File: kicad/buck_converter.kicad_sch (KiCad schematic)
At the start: 47 parts, among them J5 SolderPad, J6 SolderPad, Q2 BSZ146N10LS5, Q3 BSZ146N10LS5, U2 LM5146

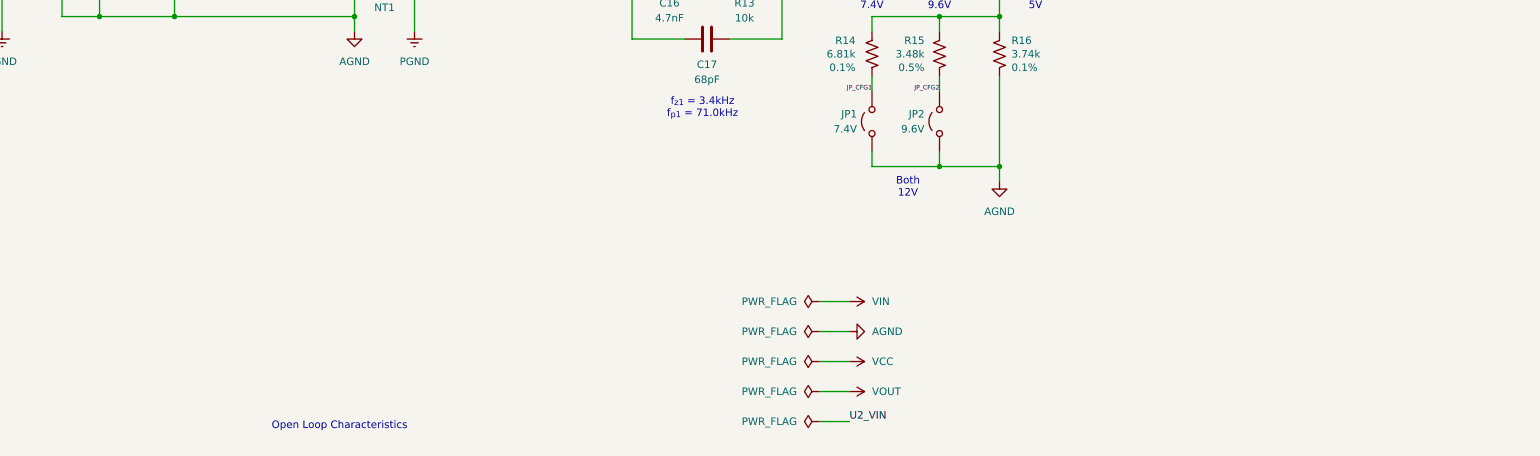
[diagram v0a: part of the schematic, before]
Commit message: Added UBCO trademark notice, prepared for production
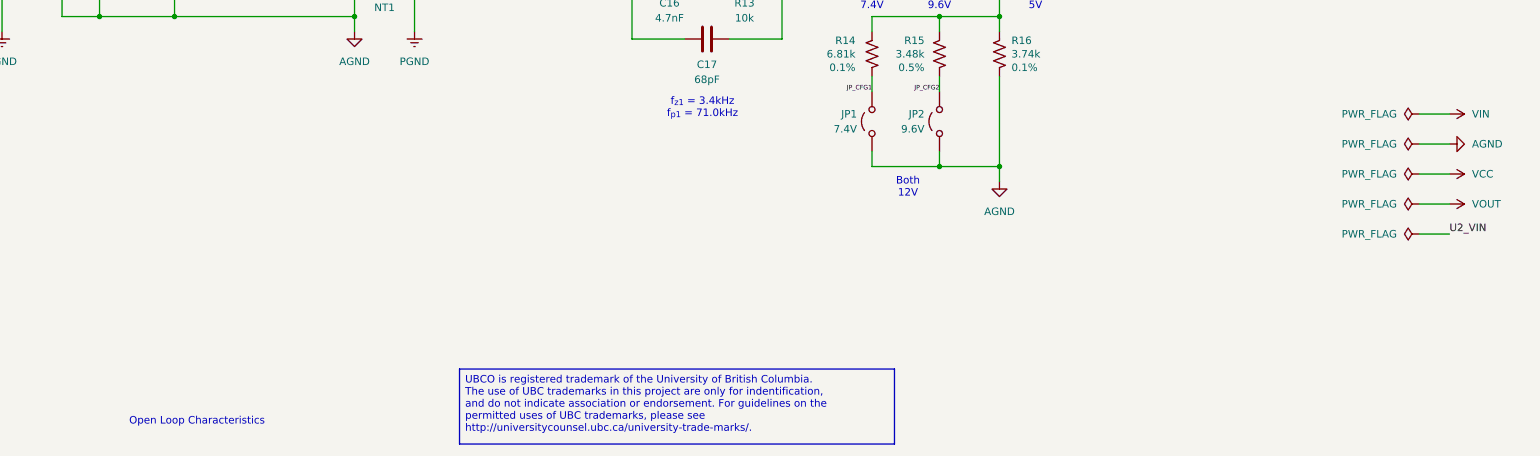
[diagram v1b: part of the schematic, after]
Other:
- company: Author: Julian Joaquin -> UBCO Aerospace
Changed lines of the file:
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@@
 		(date "2026-02-06")
 		(rev "D")
-		(company "Author: Julian Joaquin")
+		(company "UBCO Aerospace")
 		(comment 1 "Licensed under CERN-OHL-W version 2")
 		(comment 2 "Copyright © Julian Joaquin, 2026")
@@
 	(text "Open Loop Characteristics"
 		(exclude_from_sim no)
-		(at 80.01 192.532 0)
+		(at 55.88 191.77 0)
 		(effects
 			(font
@@
 		)
 	)
+	(text_box "UBCO is registered trademark of the University of British Columbia.\nThe use of UBC trademarks in this project are only for indentification,\nand do not indicate association or endorsement. For guidelines on the\npermitted uses of UBC trademarks, please see\nhttp://universitycounsel.ubc.ca/university-trade-marks/."
+		(exclude_from_sim no)
+		(at 100.33 182.88 0)
+		(size 73.66 12.7)
+		(margins 0.9525 0.9525 0.9525 0.9525)
+		(stroke
+			(width 0)
+			(type solid)
+			(color 132 0 0 1)
+		)
+		(fill
+			(type none)
+		)
+		(effects
+			(font
+				(size 1.27 1.27)
+				(color 132 0 0 1)
+			)
+			(justify left top)
+			(href "http://universitycounsel.ubc.ca/university-trade-marks")
+		)
+	)
 	(junction
 		(at 191.77 111.76)
@@
 	(wire
 		(pts
-			(xy 161.29 181.61) (xy 166.37 181.61)
+			(xy 262.89 149.86) (xy 267.97 149.86)
 		)
 		(stroke
@@
 	(wire
 		(pts
-			(xy 161.29 191.77) (xy 166.37 191.77)
+			(xy 262.89 160.02) (xy 267.97 160.02)
 		)
 		(stroke
@@
 	(wire
 		(pts
-			(xy 161.29 176.53) (xy 166.37 176.53)
+			(xy 262.89 144.78) (xy 267.97 144.78)
 		)
 		(stroke
@@
 	(wire
 		(pts
-			(xy 161.29 186.69) (xy 166.37 186.69)
+			(xy 262.89 154.94) (xy 267.97 154.94)
 		)
 		(stroke
@@
 	(wire
 		(pts
-			(xy 161.29 171.45) (xy 166.37 171.45)
+			(xy 262.89 139.7) (xy 267.97 139.7)
 		)
 		(stroke
@@
 	)
 	(image
-		(at 80.01 162.56)
+		(at 55.88 161.798)
 		(scale 0.29478)
 		(data "iVBORw0KGgoAAAANSUhEUgAABDcAAAKmCAIAAADWxeJcAAAAA3NCSVQICAjb4U/gAAAACXBIWXMA"
@@
 	)
 	(label "U2_VIN"
-		(at 166.37 191.77 0)
+		(at 267.97 160.02 0)
 		(effects
 			(font
@@
 	(symbol
 		(lib_id "power:PWR_FLAG")
-		(at 161.29 171.45 90)
+		(at 262.89 139.7 90)
 		(unit 1)
 		(exclude_from_sim no)
@@
 		(fields_autoplaced yes)
 		(property "Reference" "#FLG04"
-			(at 159.385 171.45 0)
+			(at 260.985 139.7 0)
 			(effects
 				(font
@@
 		)
 		(property "Value" "PWR_FLAG"
-			(at 157.48 171.45 90)
+			(at 259.08 139.7 90)
 			(effects
 				(font
@@
 		)
 		(property "Footprint" ""
-			(at 161.29 171.45 0)
+			(at 262.89 139.7 0)
 			(effects
 				(font
@@
 		)
 		(property "Datasheet" "~"
-			(at 161.29 171.45 0)
+			(at 262.89 139.7 0)
 			(effects
 				(font
@@
 		)
 		(property "Description" "Special symbol for telling ERC where power comes from"
-			(at 161.29 171.45 0)
+			(at 262.89 139.7 0)
 			(effects
 				(font
@@
 	(symbol
 		(lib_id "power:PWR_FLAG")
-		(at 161.29 176.53 90)
+		(at 262.89 144.78 90)
 		(unit 1)
 		(exclude_from_sim no)
@@
 		(fields_autoplaced yes)
 		(property "Reference" "#FLG05"
-			(at 159.385 176.53 0)
+			(at 260.985 144.78 0)
 			(effects
 				(font
@@
 		)
 		(property "Value" "PWR_FLAG"
-			(at 157.48 176.53 90)
+			(at 259.08 144.78 90)
 			(effects
 				(font
@@
 		)
 		(property "Footprint" ""
-			(at 161.29 176.53 0)
+			(at 262.89 144.78 0)
 			(effects
 				(font
@@
 		)
 		(property "Datasheet" "~"
-			(at 161.29 176.53 0)
+			(at 262.89 144.78 0)
 			(effects
 				(font
@@
 		)
 		(property "Description" "Special symbol for telling ERC where power comes from"
-			(at 161.29 176.53 0)
+			(at 262.89 144.78 0)
 			(effects
 				(font
@@
 	(symbol
 		(lib_id "power:VCC")
-		(at 166.37 181.61 270)
+		(at 267.97 149.86 270)
 		(unit 1)
 		(exclude_from_sim no)
@@
 		(fields_autoplaced yes)
 		(property "Reference" "#PWR021"
-			(at 162.56 181.61 0)
+			(at 264.16 149.86 0)
 			(effects
 				(font
@@
 		)
 		(property "Value" "VCC"
-			(at 170.18 181.61 90)
+			(at 271.78 149.86 90)
 			(effects
 				(font
@@
 		)
 		(property "Footprint" ""
-			(at 166.37 181.61 0)
+			(at 267.97 149.86 0)
 			(effects
 				(font
@@
 		)
 		(property "Datasheet" ""
-			(at 166.37 181.61 0)
+			(at 267.97 149.86 0)
 			(effects
 				(font
@@
 		)
 		(property "Description" "Power symbol creates a global label with name \"VCC\""
-			(at 166.37 181.61 0)
+			(at 267.97 149.86 0)
 			(effects
 				(font
@@
 	(symbol
 		(lib_id "power:GND")
-		(at 166.37 176.53 90)
+		(at 267.97 144.78 90)
 		(unit 1)
 		(exclude_from_sim no)
@@
 		(fields_autoplaced yes)
 		(property "Reference" "#PWR020"
-			(at 172.72 176.53 0)
+			(at 274.32 144.78 0)
 			(effects
 				(font
@@
 		)
 		(property "Value" "AGND"
-			(at 170.18 176.53 90)
+			(at 271.78 144.78 90)
 			(effects
 				(font
@@
 		)
 		(property "Footprint" ""
-			(at 166.37 176.53 0)
+			(at 267.97 144.78 0)
 			(effects
 				(font
@@
 		)
 		(property "Datasheet" ""
-			(at 166.37 176.53 0)
+			(at 267.97 144.78 0)
 			(effects
 				(font
@@
 		)
 		(property "Description" "Power symbol creates a global label with name \"GND\" , ground"
-			(at 166.37 176.53 0)
+			(at 267.97 144.78 0)
 			(effects
 				(font
@@
 	(symbol
 		(lib_id "power:PWR_FLAG")
-		(at 161.29 181.61 90)
+		(at 262.89 149.86 90)
 		(unit 1)
 		(exclude_from_sim no)
@@
 		(fields_autoplaced yes)
 		(property "Reference" "#FLG06"
-			(at 159.385 181.61 0)
+			(at 260.985 149.86 0)
 			(effects
 				(font
@@
 		)
 		(property "Value" "PWR_FLAG"
-			(at 157.48 181.61 90)
+			(at 259.08 149.86 90)
 			(effects
 				(font
@@
 		)
 		(property "Footprint" ""
-			(at 161.29 181.61 0)
+			(at 262.89 149.86 0)
 			(effects
 				(font
@@
 		)
 		(property "Datasheet" "~"
-			(at 161.29 181.61 0)
+			(at 262.89 149.86 0)
 			(effects
 				(font
@@
 		)
 		(property "Description" "Special symbol for telling ERC where power comes from"
-			(at 161.29 181.61 0)
+			(at 262.89 149.86 0)
 			(effects
 				(font
@@
 	(symbol
 		(lib_id "power:VCC")
-		(at 166.37 171.45 270)
+		(at 267.97 139.7 270)
 		(unit 1)
 		(exclude_from_sim no)
@@
 		(fields_autoplaced yes)
 		(property "Reference" "#PWR019"
-			(at 162.56 171.45 0)
+			(at 264.16 139.7 0)
 			(effects
 				(font
@@
 		)
 		(property "Value" "VIN"
-			(at 170.18 171.45 90)
+			(at 271.78 139.7 90)
 			(effects
 				(font
@@
 		)
 		(property "Footprint" ""
-			(at 166.37 171.45 0)
+			(at 267.97 139.7 0)
 			(effects
 				(font
@@
 		)
 		(property "Datasheet" ""
-			(at 166.37 171.45 0)
+			(at 267.97 139.7 0)
 			(effects
 				(font
@@
 		)
 		(property "Description" "Power symbol creates a global label with name \"VCC\""
-			(at 166.37 171.45 0)
+			(at 267.97 139.7 0)
 			(effects
 				(font
@@
 	(symbol
 		(lib_id "power:PWR_FLAG")
-		(at 161.29 186.69 90)
+		(at 262.89 154.94 90)
 		(unit 1)
 		(exclude_from_sim no)
@@
 		(fields_autoplaced yes)
 		(property "Reference" "#FLG07"
-			(at 159.385 186.69 0)
+			(at 260.985 154.94 0)
 			(effects
 				(font
@@
 		)
 		(property "Value" "PWR_FLAG"
-			(at 157.48 186.69 90)
+			(at 259.08 154.94 90)
 			(effects
 				(font
@@
 		)
 		(property "Footprint" ""
-			(at 161.29 186.69 0)
+			(at 262.89 154.94 0)
 			(effects
 				(font
@@
 		)
 		(property "Datasheet" "~"
-			(at 161.29 186.69 0)
+			(at 262.89 154.94 0)
 			(effects
 				(font
@@
 		)
 		(property "Description" "Special symbol for telling ERC where power comes from"
-			(at 161.29 186.69 0)
+			(at 262.89 154.94 0)
 			(effects
 				(font
@@
 	(symbol
 		(lib_id "power:PWR_FLAG")
-		(at 161.29 191.77 90)
+		(at 262.89 160.02 90)
 		(unit 1)
 		(exclude_from_sim no)
@@
 		(fields_autoplaced yes)
 		(property "Reference" "#FLG08"
-			(at 159.385 191.77 0)
+			(at 260.985 160.02 0)
 			(effects
 				(font
@@
 		)
 		(property "Value" "PWR_FLAG"
-			(at 157.48 191.77 90)
+			(at 259.08 160.02 90)
 			(effects
 				(font
@@
 		)
 		(property "Footprint" ""
-			(at 161.29 191.77 0)
+			(at 262.89 160.02 0)
 			(effects
 				(font
@@
 		)
 		(property "Datasheet" "~"
-			(at 161.29 191.77 0)
+			(at 262.89 160.02 0)
 			(effects
 				(font
@@
 		)
 		(property "Description" "Special symbol for telling ERC where power comes from"
-			(at 161.29 191.77 0)
+			(at 262.89 160.02 0)
 			(effects
 				(font
@@
 	(symbol
 		(lib_id "power:VDD")
-		(at 166.37 186.69 270)
+		(at 267.97 154.94 270)
 		(unit 1)
 		(exclude_from_sim no)
@@
 		(fields_autoplaced yes)
 		(property "Reference" "#PWR022"
-			(at 162.56 186.69 0)
+			(at 264.16 154.94 0)
 			(effects
 				(font
@@
 		)
 		(property "Value" "VOUT"
-			(at 170.18 186.69 90)
+			(at 271.78 154.94 90)
 			(effects
 				(font
@@
 		)
 		(property "Footprint" ""
-			(at 166.37 186.69 0)
+			(at 267.97 154.94 0)
 			(effects
 				(font
@@
 		)
 		(property "Datasheet" ""
-			(at 166.37 186.69 0)
+			(at 267.97 154.94 0)
 			(effects
 				(font
@@
 		)
 		(property "Description" "Power symbol creates a global label with name \"VDD\""
-			(at 166.37 186.69 0)
+			(at 267.97 154.94 0)
 			(effects
 				(font

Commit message: Final production files
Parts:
- D4: FT Rotation Offset 0 -> 180

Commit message: Component optimizations
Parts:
- C18, C19, C20, C21, C22, C23: footprint Capacitor_SMD:C_1206_3216Metric -> Capacitor_SMD:C_1206_3216Metric_Pad1.33x1.80mm_HandSolder; now left out of the parts list
- C24, L1: now left out of the parts list
- R16: footprint Resistor_SMD:R_0603_1608Metric -> Resistor_SMD:R_0603_1608Metric_Pad0.98x0.95mm_HandSolder; now left out of the parts list
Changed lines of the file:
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@@
 		(unit 1)
 		(exclude_from_sim no)
-		(in_bom yes)
+		(in_bom no)
 		(on_board yes)
 		(dnp no)
@@
 			)
 		)
-		(property "Footprint" "Capacitor_SMD:C_1206_3216Metric"
+		(property "Footprint" "Capacitor_SMD:C_1206_3216Metric_Pad1.33x1.80mm_HandSolder"
 			(at 221.9452 93.98 0)
 			(effects
@@
 		(unit 1)
 		(exclude_from_sim no)
-		(in_bom yes)
+		(in_bom no)
 		(on_board yes)
 		(dnp no)
@@
 			)
 		)
-		(property "Footprint" "Capacitor_SMD:C_1206_3216Metric"
+		(property "Footprint" "Capacitor_SMD:C_1206_3216Metric_Pad1.33x1.80mm_HandSolder"
 			(at 202.8952 93.98 0)
 			(effects
@@
 		(unit 1)
 		(exclude_from_sim no)
-		(in_bom yes)
+		(in_bom no)
 		(on_board yes)
 		(dnp no)
@@
 			)
 		)
-		(property "Footprint" "Resistor_SMD:R_0603_1608Metric"
+		(property "Footprint" "Resistor_SMD:R_0603_1608Metric_Pad0.98x0.95mm_HandSolder"
 			(at 190.754 129.794 90)
 			(effects
@@
 		(unit 1)
 		(exclude_from_sim no)
-		(in_bom yes)
+		(in_bom no)
 		(on_board yes)
 		(dnp no)
@@
 		(unit 1)
 		(exclude_from_sim no)
-		(in_bom yes)
+		(in_bom no)
 		(on_board yes)
 		(dnp no)
@@
 		(unit 1)
 		(exclude_from_sim no)
-		(in_bom yes)
+		(in_bom no)
 		(on_board yes)
 		(dnp no)
@@
 			)
 		)
-		(property "Footprint" "Capacitor_SMD:C_1206_3216Metric"
+		(property "Footprint" "Capacitor_SMD:C_1206_3216Metric_Pad1.33x1.80mm_HandSolder"
 			(at 228.2952 93.98 0)
 			(effects
@@
 		(unit 1)
 		(exclude_from_sim no)
-		(in_bom yes)
+		(in_bom no)
 		(on_board yes)
 		(dnp no)
@@
 			)
 		)
-		(property "Footprint" "Capacitor_SMD:C_1206_3216Metric"
+		(property "Footprint" "Capacitor_SMD:C_1206_3216Metric_Pad1.33x1.80mm_HandSolder"
 			(at 215.5952 93.98 0)
 			(effects
@@
 		(unit 1)
 		(exclude_from_sim no)
-		(in_bom yes)
+		(in_bom no)
 		(on_board yes)
 		(dnp no)
@@
 			)
 		)
-		(property "Footprint" "Capacitor_SMD:C_1206_3216Metric"
+		(property "Footprint" "Capacitor_SMD:C_1206_3216Metric_Pad1.33x1.80mm_HandSolder"
 			(at 234.6452 93.98 0)
 			(effects
@@
 		(unit 1)
 		(exclude_from_sim no)
-		(in_bom yes)
+		(in_bom no)
 		(on_board yes)
 		(dnp no)
@@
 			)
 		)
-		(property "Footprint" "Capacitor_SMD:C_1206_3216Metric"
+		(property "Footprint" "Capacitor_SMD:C_1206_3216Metric_Pad1.33x1.80mm_HandSolder"
 			(at 209.2452 93.98 0)
 			(effects
